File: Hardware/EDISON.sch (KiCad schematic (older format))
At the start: 2 parts

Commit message: Updated I2C pullup resistors and labels
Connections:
- wire segments 107 -> 98
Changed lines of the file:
@@
 $Descr A4 8268 11693 portrait
 encoding utf-8
-Sheet 10 10
+Sheet 8 10
 Title ""
 Date ""
@@
 	3350 5450 3450 5450
 Wire Wire Line
-	3350 5450 3350 5550
-Wire Wire Line
-	3350 5550 3350 5650
-Wire Wire Line
-	3350 5650 3350 5750
-Wire Wire Line
-	3350 5750 3350 5850
-Wire Wire Line
-	3350 5850 3350 5950
-Wire Wire Line
-	3350 5950 3350 6200
+	3350 5450 3350 6200
 Connection ~ 3350 1850
 Wire Wire Line
@@
 Connection ~ 3350 1650
 Wire Wire Line
-	3350 1400 3350 1650
-Wire Wire Line
-	3350 1650 3350 1750
-Wire Wire Line
-	3350 1750 3350 1850
-Wire Wire Line
-	3350 1850 3350 1950
+	3350 1400 3350 1950
 Wire Wire Line
 	3350 1750 3450 1750
@@
 	5450 4550 6050 4550
 Wire Wire Line
-	1350 1850 1350 1950
-Wire Wire Line
-	1350 1950 1350 2050
+	1350 1850 1350 2050
 Wire Wire Line
 	1350 1950 1250 1950

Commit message: Made design review fixes, added breakouts
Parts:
- gave numbers to parts that had none: 2
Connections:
- net labels added: MCU_GPIO_X_1, MCU_GPIO_X_10/PWM1, MCU_GPIO_X_11/PWM2, MCU_GPIO_X_12/PWM3, MCU_GPIO_X_13/PWM4, MCU_GPIO_X_2, MCU_GPIO_X_3/UART_RX, MCU_GPIO_X_4/UART_TX, MCU_GPIO_X_5, MCU_GPIO_X_6, MCU_GPIO_X_7, MCU_GPIO_X_8, MCU_GPIO_X_9
- wire segments 98 -> 133
- no-connect marks 28 -> 15

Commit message: Annotated schematic
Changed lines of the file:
@@
 LIBS:microchip_pic18mcu
 LIBS:microchip
+LIBS:microchip1
 LIBS:microcontrollers
 LIBS:motorola
@@
 LIBS:sensors
 LIBS:siliconi
+LIBS:special
 LIBS:stm8
 LIBS:stm32
@@
 To DFE\n(IADC/\n DAC/\n SPDIF)
 $Comp
-L +1.8VSB #PWR118
+L +1.8VSB #PWR0104
 U 1 1 57F8CABA
 P 3150 1400
-F 0 "#PWR118" H 3150 1540 20  0001 C CNN
+F 0 "#PWR0104" H 3150 1540 20  0001 C CNN
 F 1 "+1.8VSB" H 3150 1510 30  0000 C CNN
 F 2 "" H 3150 1400 60  0000 C CNN
@@
 $EndComp
 $Comp
-L +3.3VSB #PWR119
+L +3.3VSB #PWR0105
 U 1 1 57F8CAC0
 P 3350 1400
-F 0 "#PWR119" H 3350 1360 30  0001 C CNN
+F 0 "#PWR0105" H 3350 1360 30  0001 C CNN
 F 1 "+3.3VSB" H 3350 1510 30  0000 C CNN
 F 2 "" H 3350 1400 60  0000 C CNN
@@
 NoConn ~ 1250 1750
 $Comp
-L GND-RESCUE-museV2 #PWR117
+L GND-RESCUE-museV2-RESCUE-museV2 #PWR0106
 U 1 1 57F8CACB
 P 1350 2050
-F 0 "#PWR117" H 1350 2050 30  0001 C CNN
+F 0 "#PWR0106" H 1350 2050 30  0001 C CNN
 F 1 "GND" H 1350 1980 30  0001 C CNN
 F 2 "" H 1350 2050 60  0000 C CNN
@@
 Intel Edison Connection
 $Comp
-L GND-RESCUE-museV2 #PWR120
+L GND-RESCUE-museV2-RESCUE-museV2 #PWR0107
 U 1 1 57F8CAEE
 P 3350 6200
-F 0 "#PWR120" H 3350 6200 30  0001 C CNN
+F 0 "#PWR0107" H 3350 6200 30  0001 C CNN
 F 1 "GND" H 3350 6130 30  0001 C CNN
 F 2 "" H 3350 6200 60  0000 C CNN

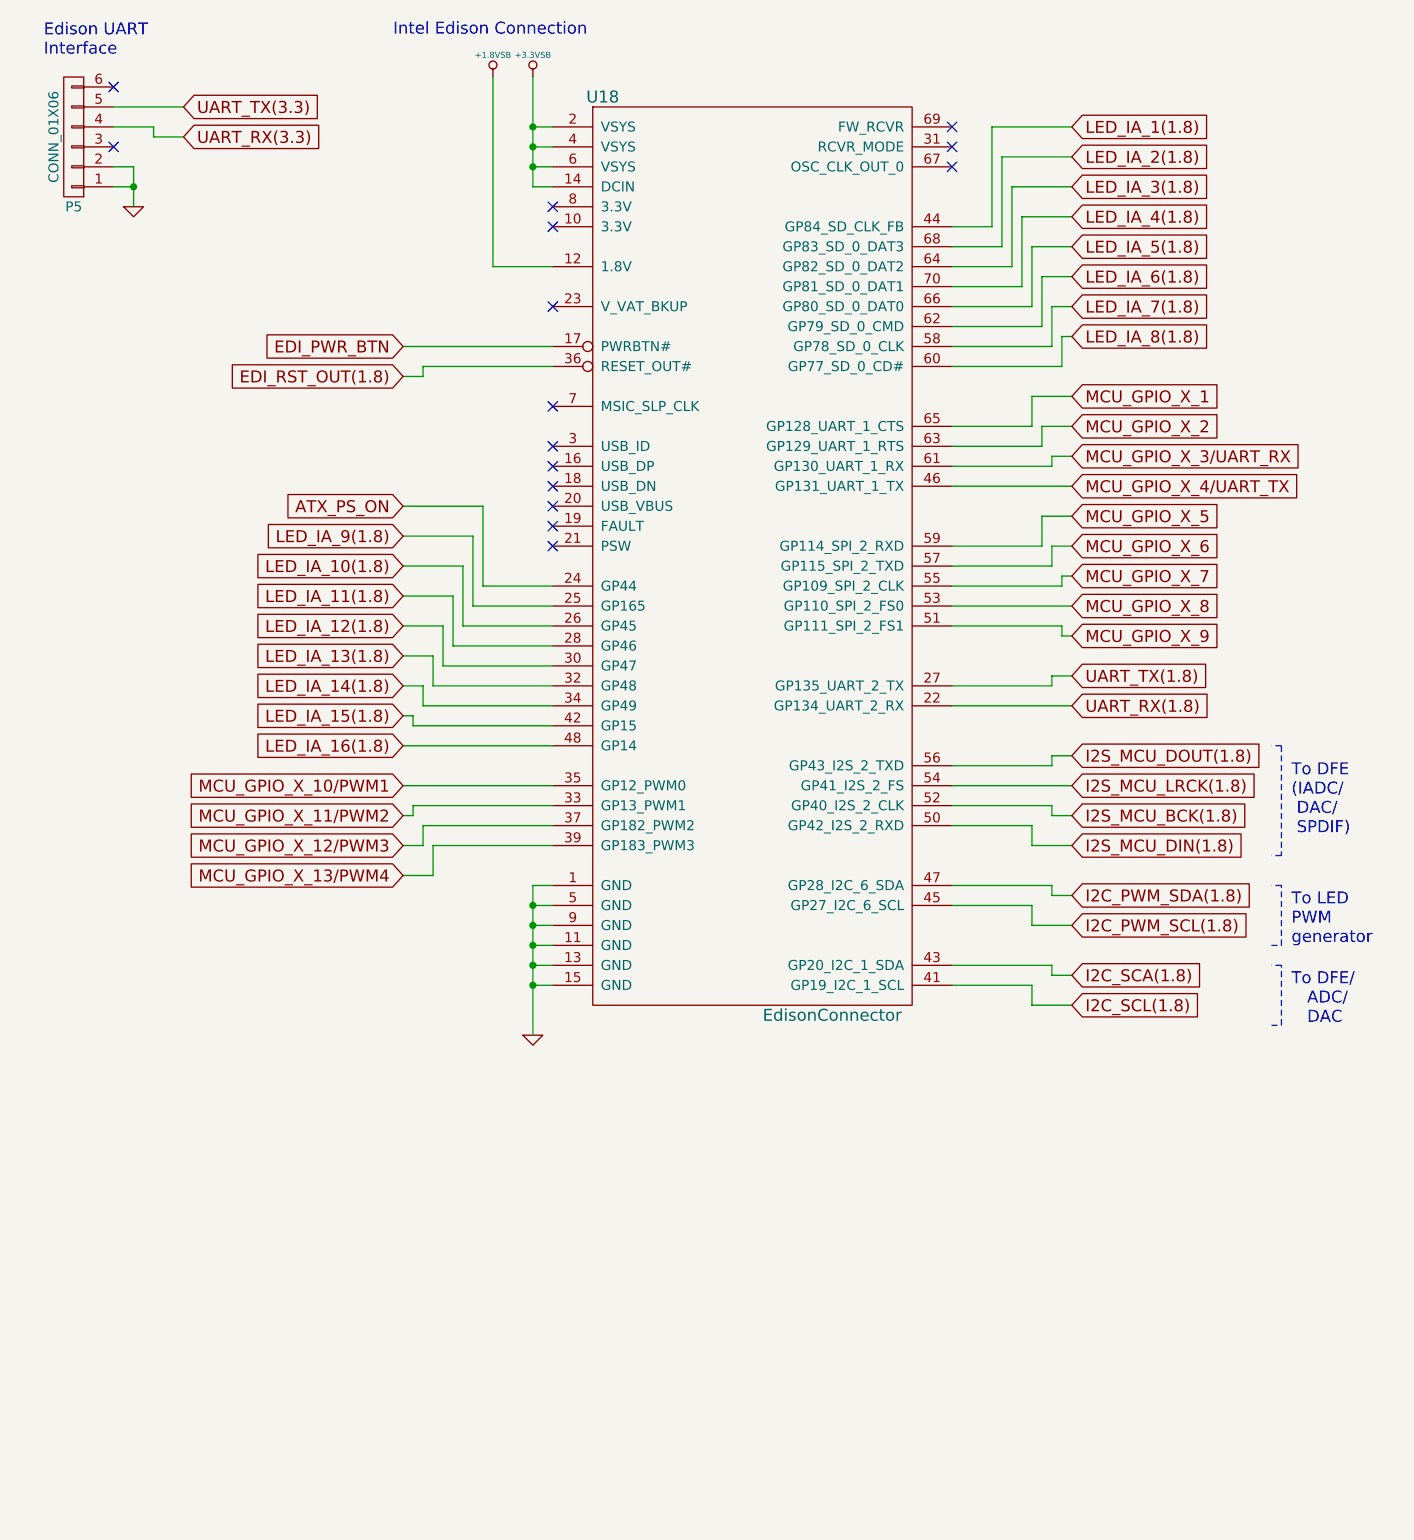
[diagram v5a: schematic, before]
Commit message: Added bluetooth pair button
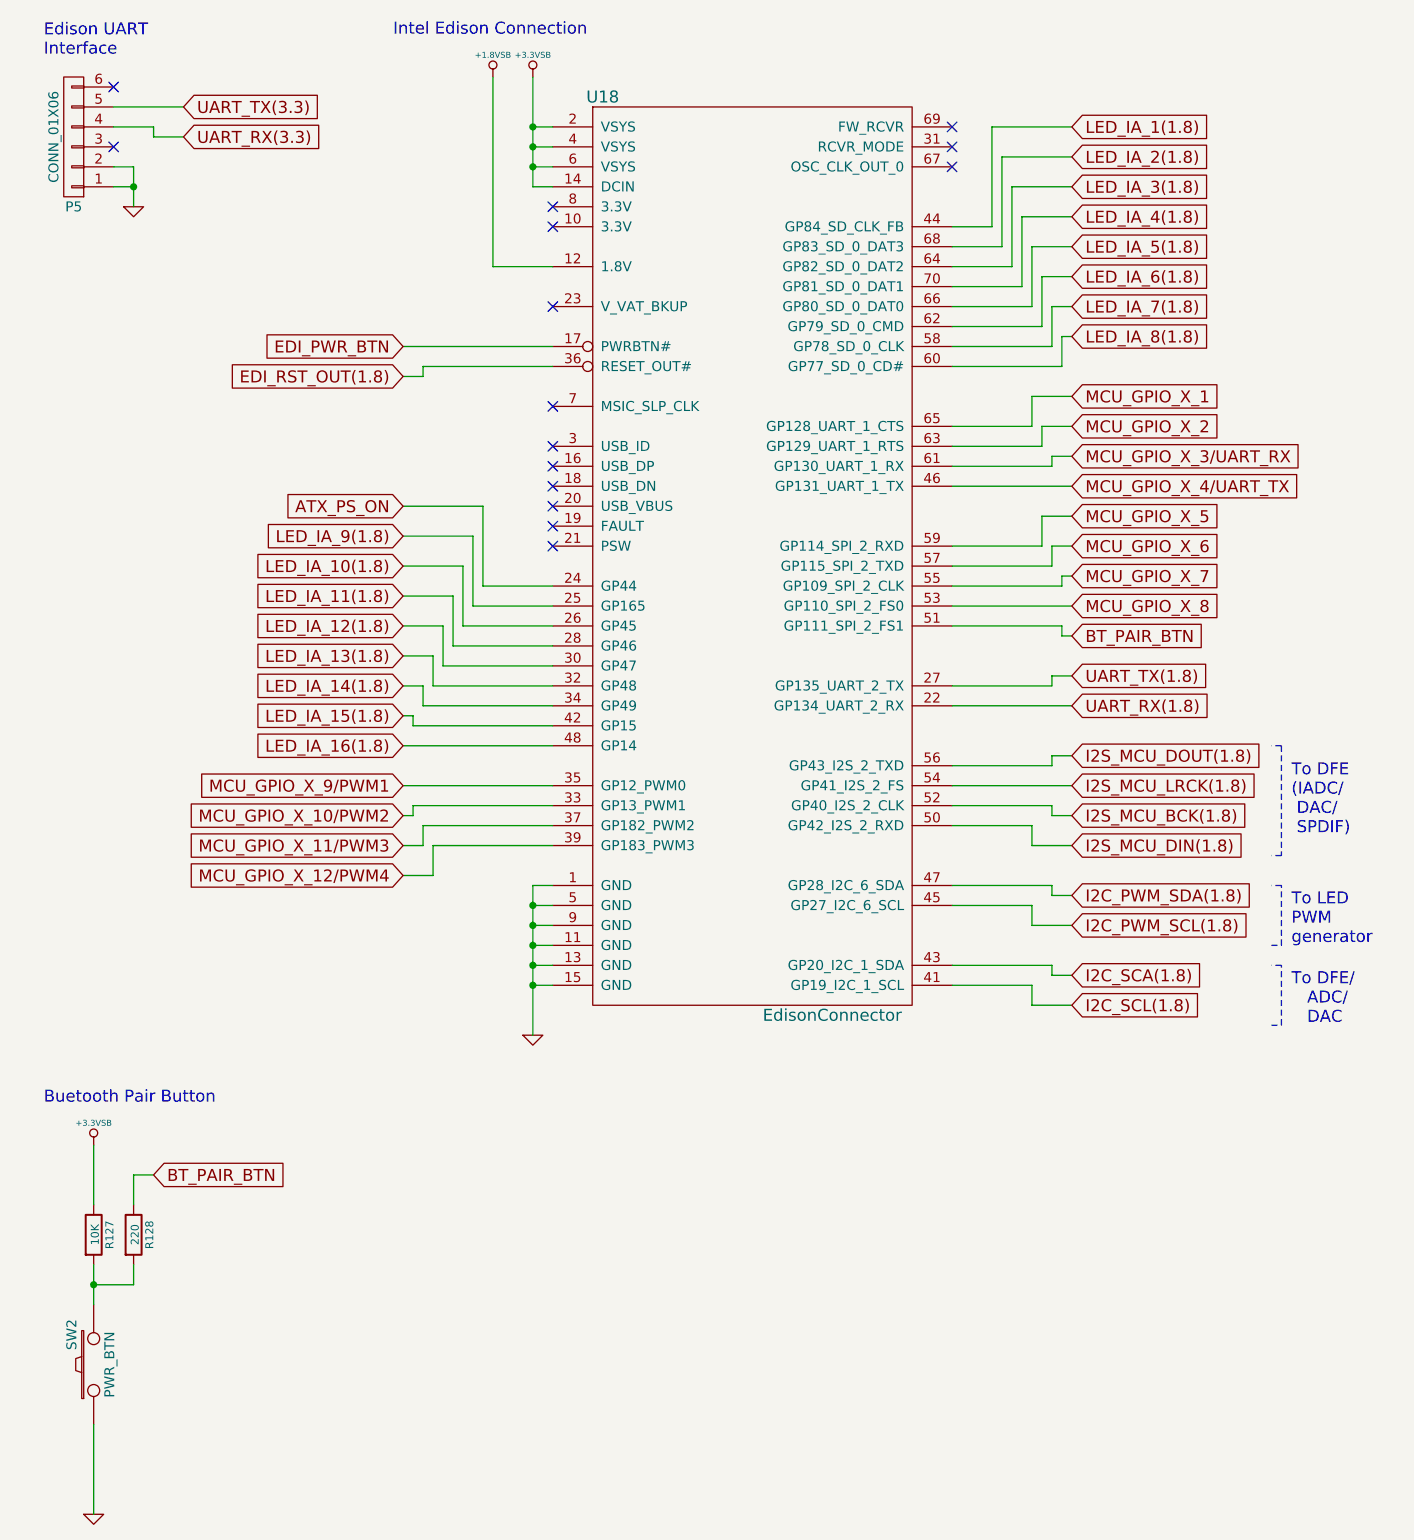
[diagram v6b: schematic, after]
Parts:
- added R127: 10K, symbol R-RESCUE-museV2
- added R128: 220, symbol R-RESCUE-museV2
- added SW2: PWR_BTN, symbol SW_PUSH
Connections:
- net +3.3VSB: now also R127.1
- net GND: now also SW2.1
- net MCU_GPIO_X_10/PWM1 renamed MCU_GPIO_X_9/PWM1
- net MCU_GPIO_X_11/PWM2 renamed MCU_GPIO_X_10/PWM2
- net MCU_GPIO_X_12/PWM3 renamed MCU_GPIO_X_11/PWM3
- net MCU_GPIO_X_13/PWM4 renamed MCU_GPIO_X_12/PWM4
- net MCU_GPIO_X_9 renamed BT_PAIR_BTN
- net BT_PAIR_BTN: now also R128.1
- new net: R127.2, R128.2, SW2.2
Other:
- note added: "Buetooth Pair Button"
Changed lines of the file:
@@
 To DFE\n(IADC/\n DAC/\n SPDIF)
 $Comp
-L +1.8VSB #PWR0103
+L +1.8VSB #PWR112
 U 1 1 57F8CABA
 P 3150 1400
-F 0 "#PWR0103" H 3150 1540 20  0001 C CNN
+F 0 "#PWR112" H 3150 1540 20  0001 C CNN
 F 1 "+1.8VSB" H 3150 1510 30  0000 C CNN
 F 2 "" H 3150 1400 60  0000 C CNN
@@
 $EndComp
 $Comp
-L +3.3VSB #PWR0104
+L +3.3VSB #PWR113
 U 1 1 57F8CAC0
 P 3350 1400
-F 0 "#PWR0104" H 3350 1360 30  0001 C CNN
+F 0 "#PWR113" H 3350 1360 30  0001 C CNN
 F 1 "+3.3VSB" H 3350 1510 30  0000 C CNN
 F 2 "" H 3350 1400 60  0000 C CNN
@@
 NoConn ~ 1250 1750
 $Comp
-L GND-RESCUE-museV2-RESCUE-museV2 #PWR0105
+L GND-RESCUE-museV2-RESCUE-museV2 #PWR114
 U 1 1 57F8CACB
 P 1350 2050
-F 0 "#PWR0105" H 1350 2050 30  0001 C CNN
+F 0 "#PWR114" H 1350 2050 30  0001 C CNN
 F 1 "GND" H 1350 1980 30  0001 C CNN
 F 2 "" H 1350 2050 60  0000 C CNN
@@
 Intel Edison Connection
 $Comp
-L GND-RESCUE-museV2-RESCUE-museV2 #PWR0106
+L GND-RESCUE-museV2-RESCUE-museV2 #PWR115
 U 1 1 57F8CAEE
 P 3350 6200
-F 0 "#PWR0106" H 3350 6200 30  0001 C CNN
+F 0 "#PWR115" H 3350 6200 30  0001 C CNN
 F 1 "GND" H 3350 6130 30  0001 C CNN
 F 2 "" H 3350 6200 60  0000 C CNN
@@
 MCU_GPIO_X_8
 Text GLabel 6050 4200 2    60   Input ~ 0
-MCU_GPIO_X_9
+BT_PAIR_BTN
 Wire Wire Line
 	5450 4150 6000 4150
@@
 	3100 3950 3450 3950
 Text GLabel 2700 4950 0    60   Input ~ 0
-MCU_GPIO_X_10/PWM1
+MCU_GPIO_X_9/PWM1
 Wire Wire Line
 	2700 4950 3450 4950
 Text GLabel 2700 5100 0    60   Input ~ 0
-MCU_GPIO_X_11/PWM2
+MCU_GPIO_X_10/PWM2
 Text GLabel 2700 5250 0    60   Input ~ 0
-MCU_GPIO_X_12/PWM3
+MCU_GPIO_X_11/PWM3
 Text GLabel 2700 5400 0    60   Input ~ 0
-MCU_GPIO_X_13/PWM4
+MCU_GPIO_X_12/PWM4
 Wire Wire Line
 	2700 5100 2750 5100
@@
 Wire Wire Line
 	2850 5250 3450 5250
+$Comp
+L GND-RESCUE-museV2-RESCUE-museV2 #PWR117
+U 1 1 58589956
+P 1150 8600
+F 0 "#PWR117" H 1150 8600 30  0001 C CNN
+F 1 "GND" H 1150 8530 30  0001 C CNN
+F 2 "" H 1150 8600 60  0000 C CNN
+F 3 "" H 1150 8600 60  0000 C CNN
+	1    1150 8600
+	1    0    0    -1
+$EndComp
+$Comp
+L R-RESCUE-museV2 R127
+U 1 1 5858995C
+P 1150 7200
+F 0 "R127" V 1230 7200 40  0000 C CNN
+F 1 "10K" V 1157 7201 40  0000 C CNN
+F 2 "" V 1080 7200 30  0000 C CNN
+F 3 "" H 1150 7200 30  0000 C CNN
+	1    1150 7200
+	1    0    0    -1
+$EndComp
+$Comp
+L SW_PUSH SW2
+U 1 1 58589963
+P 1150 7850
+F 0 "SW2" H 1300 7960 50  0000 C CNN
+F 1 "PWR_BTN" H 1150 7770 50  0000 C CNN
+F 2 "" H 1150 7850 60  0000 C CNN
+F 3 "" H 1150 7850 60  0000 C CNN
+	1    1150 7850
+	0    -1   -1   0
+$EndComp
+Wire Wire Line
+	1150 8600 1150 8150
+Wire Wire Line
+	1150 6750 1150 7050
+Connection ~ 1150 7450
+Wire Wire Line
+	1150 7350 1150 7550
+$Comp
+L R-RESCUE-museV2 R128
+U 1 1 5858996E
+P 1350 7200
+F 0 "R128" V 1430 7200 40  0000 C CNN
+F 1 "220" V 1357 7201 40  0000 C CNN
+F 2 "" V 1280 7200 30  0000 C CNN
+F 3 "" H 1350 7200 30  0000 C CNN
+	1    1350 7200
+	1    0    0    -1
+$EndComp
+Wire Wire Line
+	1350 7450 1150 7450
+$Comp
+L +3.3VSB #PWR116
+U 1 1 58589976
+P 1150 6750
+F 0 "#PWR116" H 1150 6710 30  0001 C CNN
+F 1 "+3.3VSB" H 1150 6860 30  0000 C CNN
+F 2 "" H 1150 6750 60  0000 C CNN
+F 3 "" H 1150 6750 60  0000 C CNN
+	1    1150 6750
+	1    0    0    -1
+$EndComp
+Wire Wire Line
+	1350 7350 1350 7450
+Wire Wire Line
+	1350 6900 1350 7050
+Text GLabel 1450 6900 2    60   Input ~ 0
+BT_PAIR_BTN
+Wire Wire Line
+	1450 6900 1350 6900
+Text Notes 900  6550 0    60   ~ 0
+Buetooth Pair Button
 $EndSCHEMATC

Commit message: Fixing schematic issues
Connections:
- net MCU_GPIO_X_1 is gone; now on net MCU_GPIO_X_5: U18.65 (GP128_UART_1_CTS)
- net MCU_GPIO_X_2 is gone; now on net MCU_GPIO_X_6: U18.63 (GP129_UART_1_RTS)
- net MCU_GPIO_X_5: no longer U18.59 (GP114_SPI_2_RXD)
- net MCU_GPIO_X_6: no longer U18.57 (GP115_SPI_2_TXD)
- net ATX_PS_ON: no longer names the net of U18.24 (GP44)
- net EDI_PWR_BTN renamed EDISON_PWR_BTN
- net EDI_RST_OUT(1.8) renamed EDISON_RST_OUT
- net MCU_GPIO_X_10/PWM2 renamed MCU_GPIO_X_2/PWM2
- net MCU_GPIO_X_11/PWM3 renamed MCU_GPIO_X_3/PWM3
- net MCU_GPIO_X_12/PWM4 renamed MCU_GPIO_X_4/PWM4
- net MCU_GPIO_X_3/UART_RX renamed MCU_GPIO_X_7/UART_RX
- net MCU_GPIO_X_4/UART_TX renamed MCU_GPIO_X_8/UART_TX
- net MCU_GPIO_X_7 renamed ADC_CLKE_INT
- net MCU_GPIO_X_8 renamed ADC_ESEN_INT
- net MCU_GPIO_X_9/PWM1 renamed MCU_GPIO_X_1/PWM1
- new net MCU_GPIO_X_10: U18.57 (GP115_SPI_2_TXD)
- new net MCU_GPIO_X_9: U18.59 (GP114_SPI_2_RXD)
- no-connect marks 15 -> 16
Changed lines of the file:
@@
 To DFE\n(IADC/\n DAC/\n SPDIF)
 $Comp
-L +1.8VSB #PWR112
+L +1.8VSB #PWR097
 U 1 1 57F8CABA
 P 3150 1400
-F 0 "#PWR112" H 3150 1540 20  0001 C CNN
+F 0 "#PWR097" H 3150 1540 20  0001 C CNN
 F 1 "+1.8VSB" H 3150 1510 30  0000 C CNN
 F 2 "" H 3150 1400 60  0000 C CNN
@@
 $EndComp
 $Comp
-L +3.3VSB #PWR113
+L +3.3VSB #PWR098
 U 1 1 57F8CAC0
 P 3350 1400
-F 0 "#PWR113" H 3350 1360 30  0001 C CNN
+F 0 "#PWR098" H 3350 1360 30  0001 C CNN
 F 1 "+3.3VSB" H 3350 1510 30  0000 C CNN
 F 2 "" H 3350 1400 60  0000 C CNN
@@
 NoConn ~ 1250 1750
 $Comp
-L GND-RESCUE-museV2-RESCUE-museV2 #PWR114
+L GND-RESCUE-museV2-RESCUE-museV2 #PWR099
 U 1 1 57F8CACB
 P 1350 2050
-F 0 "#PWR114" H 1350 2050 30  0001 C CNN
+F 0 "#PWR099" H 1350 2050 30  0001 C CNN
 F 1 "GND" H 1350 1980 30  0001 C CNN
 F 2 "" H 1350 2050 60  0000 C CNN
@@
 Intel Edison Connection
 $Comp
-L GND-RESCUE-museV2-RESCUE-museV2 #PWR115
+L GND-RESCUE-museV2-RESCUE-museV2 #PWR0100
 U 1 1 57F8CAEE
 P 3350 6200
-F 0 "#PWR115" H 3350 6200 30  0001 C CNN
+F 0 "#PWR0100" H 3350 6200 30  0001 C CNN
 F 1 "GND" H 3350 6130 30  0001 C CNN
 F 2 "" H 3350 6200 60  0000 C CNN
@@
 	1450 1700 1450 1650
 Text GLabel 2700 2750 0    60   Input ~ 0
-EDI_PWR_BTN
+EDISON_PWR_BTN
 Text GLabel 2700 2900 0    60   Input ~ 0
-EDI_RST_OUT(1.8)
+EDISON_RST_OUT
 Wire Wire Line
 	2700 2900 2800 2900
@@
 Wire Wire Line
 	2800 2850 3450 2850
-Text GLabel 2700 3550 0    60   Input ~ 0
-ATX_PS_ON
 Text GLabel 2700 3700 0    60   Input ~ 0
 LED_IA_9(1.8)
@@
 	5850 5950 5450 5950
 Text GLabel 6050 3000 2    60   Input ~ 0
-MCU_GPIO_X_1
+MCU_GPIO_X_5
 Text GLabel 6050 3150 2    60   Input ~ 0
-MCU_GPIO_X_2
+MCU_GPIO_X_6
 Text GLabel 6050 3300 2    60   Input ~ 0
-MCU_GPIO_X_3/UART_RX
+MCU_GPIO_X_7/UART_RX
 Text GLabel 6050 3450 2    60   Input ~ 0
-MCU_GPIO_X_4/UART_TX
+MCU_GPIO_X_8/UART_TX
 Text GLabel 6050 3600 2    60   Input ~ 0
-MCU_GPIO_X_5
+MCU_GPIO_X_9
 Text GLabel 6050 3750 2    60   Input ~ 0
-MCU_GPIO_X_6
+MCU_GPIO_X_10
 Text GLabel 6050 3900 2    60   Input ~ 0
-MCU_GPIO_X_7
+ADC_CLKE_INT
 Text GLabel 6050 4050 2    60   Input ~ 0
-MCU_GPIO_X_8
+ADC_ESEN_INT
 Text GLabel 6050 4200 2    60   Input ~ 0
 BT_PAIR_BTN
@@
 Wire Wire Line
 	3050 3700 2700 3700
-Wire Wire Line
-	2700 3550 3100 3550
-Wire Wire Line
-	3100 3550 3100 3950
-Wire Wire Line
-	3100 3950 3450 3950
 Text GLabel 2700 4950 0    60   Input ~ 0
-MCU_GPIO_X_9/PWM1
+MCU_GPIO_X_1/PWM1
 Wire Wire Line
 	2700 4950 3450 4950
 Text GLabel 2700 5100 0    60   Input ~ 0
-MCU_GPIO_X_10/PWM2
+MCU_GPIO_X_2/PWM2
 Text GLabel 2700 5250 0    60   Input ~ 0
-MCU_GPIO_X_11/PWM3
+MCU_GPIO_X_3/PWM3
 Text GLabel 2700 5400 0    60   Input ~ 0
-MCU_GPIO_X_12/PWM4
+MCU_GPIO_X_4/PWM4
 Wire Wire Line
 	2700 5100 2750 5100
@@
 	2850 5250 3450 5250
 $Comp
-L GND-RESCUE-museV2-RESCUE-museV2 #PWR117
+L GND-RESCUE-museV2-RESCUE-museV2 #PWR0101
 U 1 1 58589956
 P 1150 8600
-F 0 "#PWR117" H 1150 8600 30  0001 C CNN
+F 0 "#PWR0101" H 1150 8600 30  0001 C CNN
 F 1 "GND" H 1150 8530 30  0001 C CNN
 F 2 "" H 1150 8600 60  0000 C CNN
@@
 	1350 7450 1150 7450
 $Comp
-L +3.3VSB #PWR116
+L +3.3VSB #PWR0102
 U 1 1 58589976
 P 1150 6750
-F 0 "#PWR116" H 1150 6710 30  0001 C CNN
+F 0 "#PWR0102" H 1150 6710 30  0001 C CNN
 F 1 "+3.3VSB" H 1150 6860 30  0000 C CNN
 F 2 "" H 1150 6750 60  0000 C CNN
@@
 Text Notes 900  6550 0    60   ~ 0
 Buetooth Pair Button
+NoConn ~ 3450 3950
 $EndSCHEMATC
